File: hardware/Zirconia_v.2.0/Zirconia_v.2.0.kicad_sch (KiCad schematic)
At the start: 82 parts, among them J1 BD125-10-A-0305-0580-L-B, P1 Red, P2 Blk, P3 Red, P4 Blk, P6 PicoBlade_53047-0210, Q1 LTR, Q2 LTR, Q3 LTR, Q4 LTR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

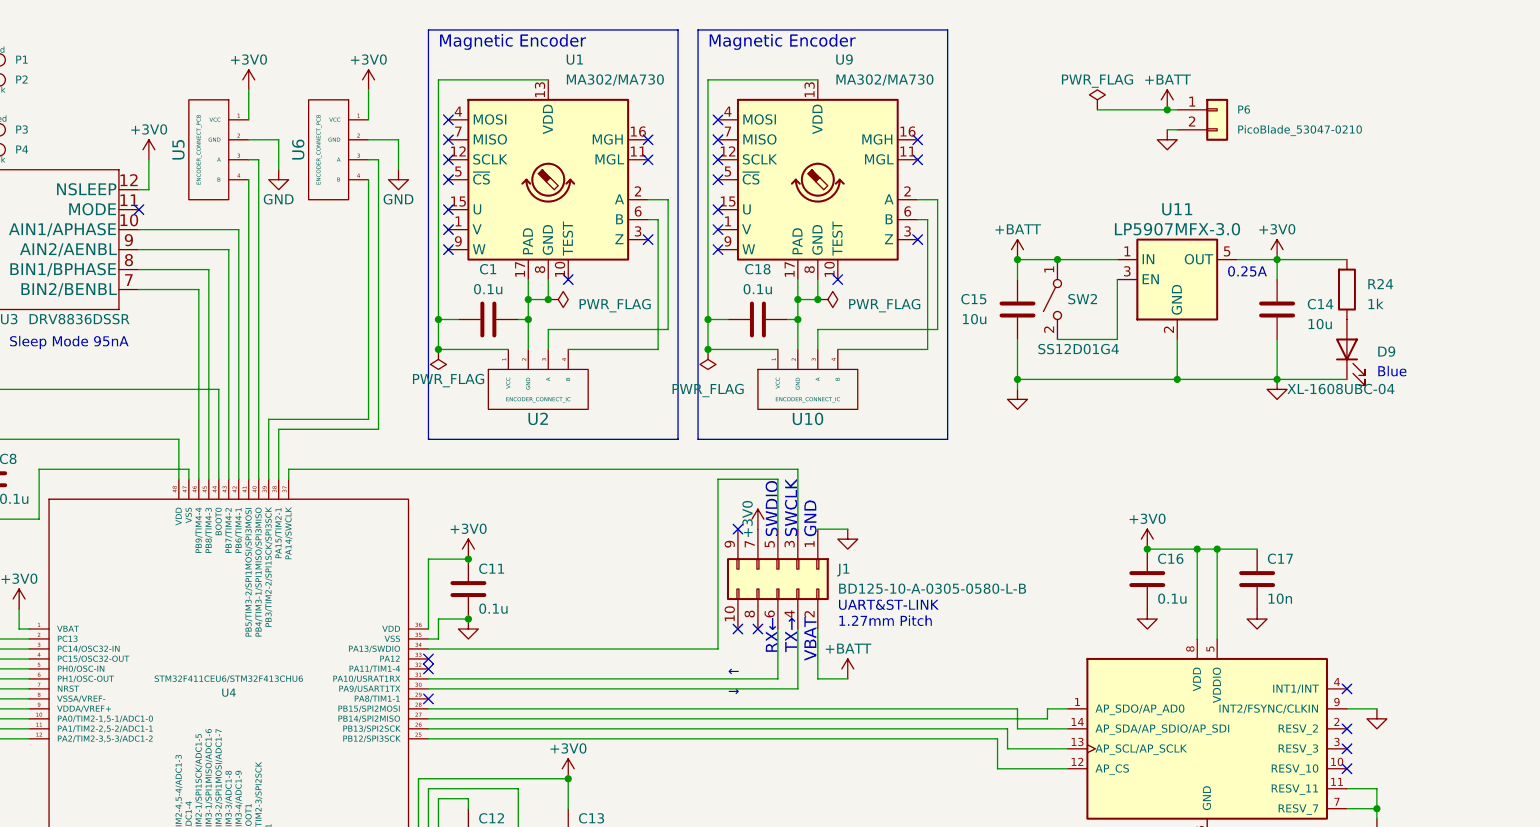
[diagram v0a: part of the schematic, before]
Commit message: JLCPCBパーツ反映
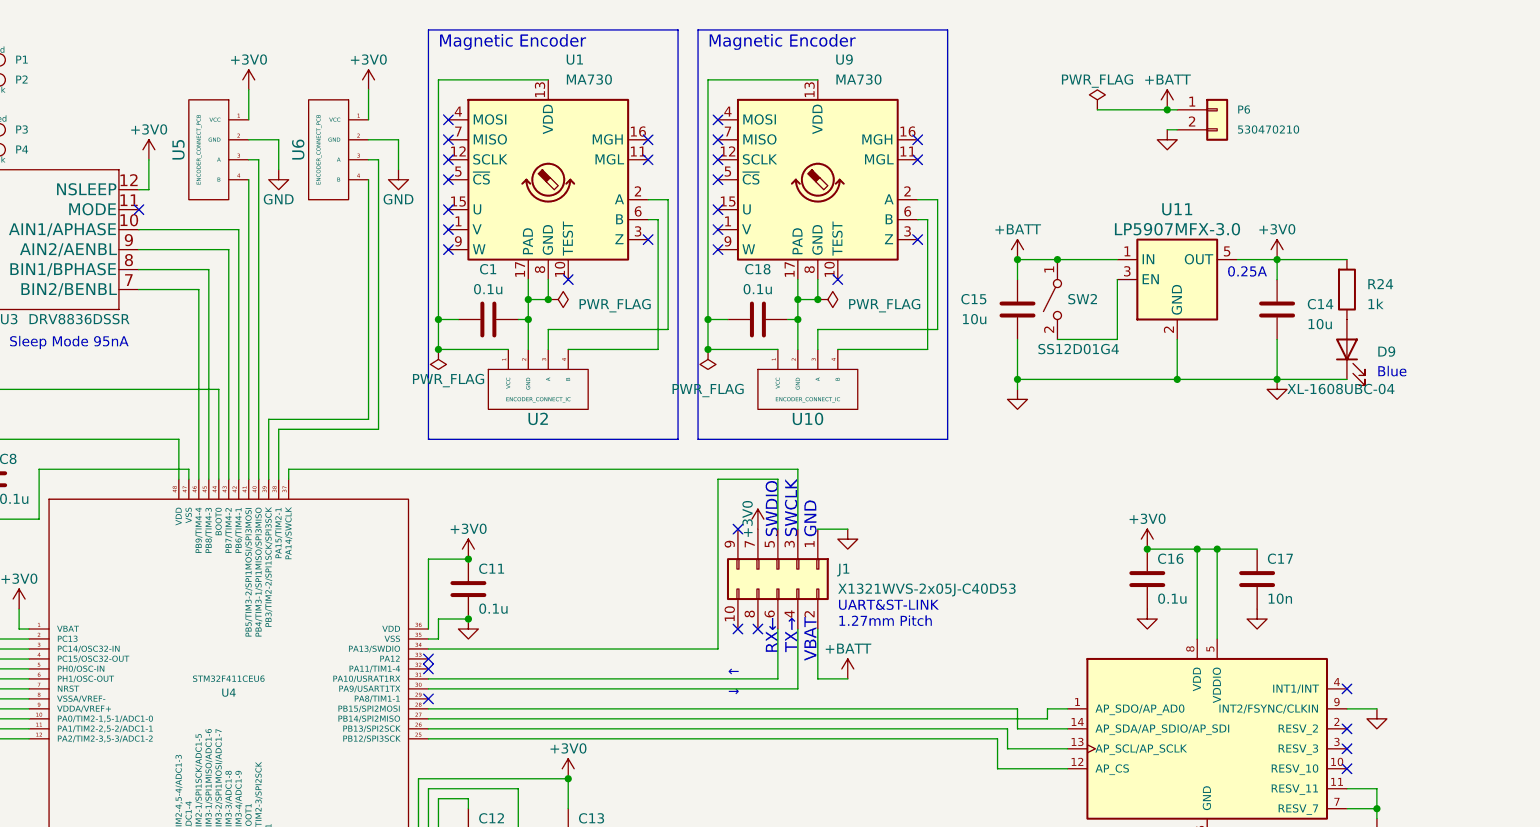
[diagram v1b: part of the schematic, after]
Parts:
- J1: value BD125-10-A-0305-0580-L-B -> X1321WVS-2x05J-C40D53; LCSC Part # (none) -> X1321WVS-2x05J-C40D53
- P6: value PicoBlade_53047-0210 -> 530470210
- U1, U9: value MA302/MA730 -> MA730
- U4: value STM32F411CEU6/STM32F413CHU6 -> STM32F411CEU6
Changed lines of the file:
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@@
 			)
 		)
-		(property "Value" "STM32F411CEU6/STM32F413CHU6"
+		(property "Value" "STM32F411CEU6"
 			(at 134.62 96.52 0)
 			(effects
@@
 			)
 		)
-		(property "Value" "BD125-10-A-0305-0580-L-B"
+		(property "Value" "X1321WVS-2x05J-C40D53"
 			(at 212.09 85.09 90)
 			(effects
@@
 			)
 		)
+		(property "LCSC Part #" "X1321WVS-2x05J-C40D53"
+			(at 204.47 82.55 0)
+			(effects
+				(font
+					(size 1.27 1.27)
+				)
+				(hide yes)
+			)
+		)
 		(pin "1"
 		)
@@
 			)
 		)
-		(property "Value" "MA302/MA730"
+		(property "Value" "MA730"
 			(at 211.7441 20.32 0)
 			(effects
@@
 			)
 		)
-		(property "Value" "PicoBlade_53047-0210"
+		(property "Value" "530470210"
 			(at 262.89 26.67 0)
 			(effects
@@
 			)
 		)
-		(property "Value" "MA302/MA730"
+		(property "Value" "MA730"
 			(at 177.4541 20.32 0)
 			(effects
